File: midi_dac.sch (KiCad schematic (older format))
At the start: 1 part

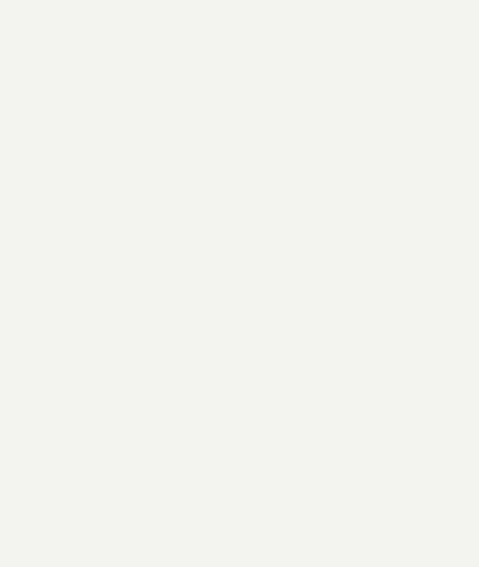
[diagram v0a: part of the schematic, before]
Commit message: Work on user io subsystem schematic
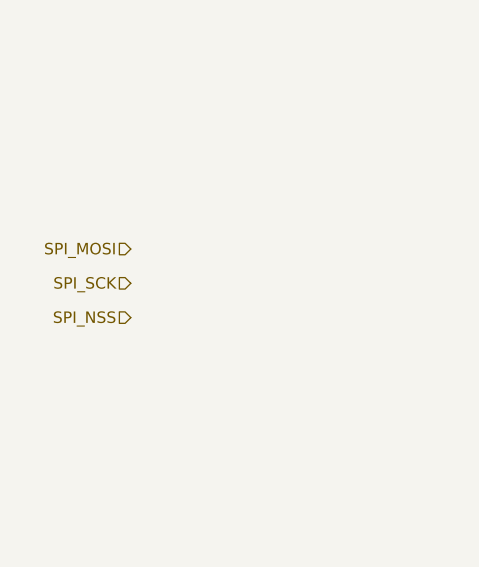
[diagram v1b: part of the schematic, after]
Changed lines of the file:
@@
 	1    0    0    -1
 $EndComp
+Text HLabel 950  2750 0    50   Input ~ 0
+SPI_MOSI
+Text HLabel 950  2900 0    50   Input ~ 0
+SPI_SCK
+Text HLabel 950  3050 0    50   Input ~ 0
+SPI_NSS
 $EndSCHEMATC

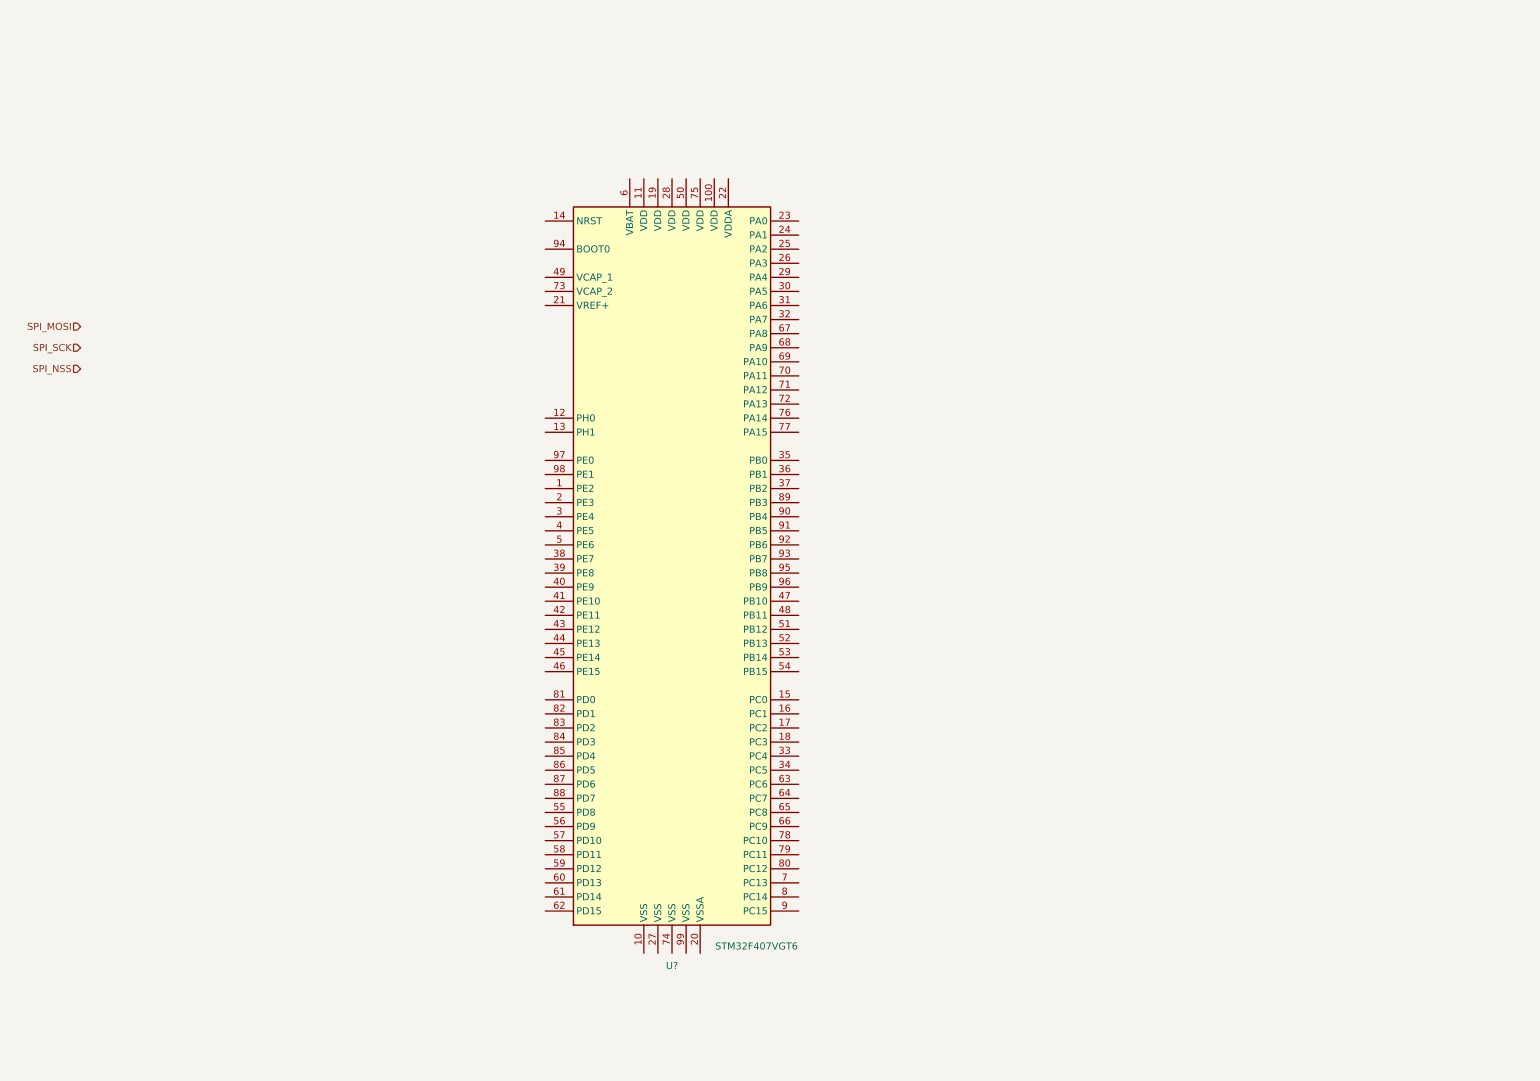
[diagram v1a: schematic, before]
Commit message: Add f4 decoupling capacitors, add dac, add power converter circuit
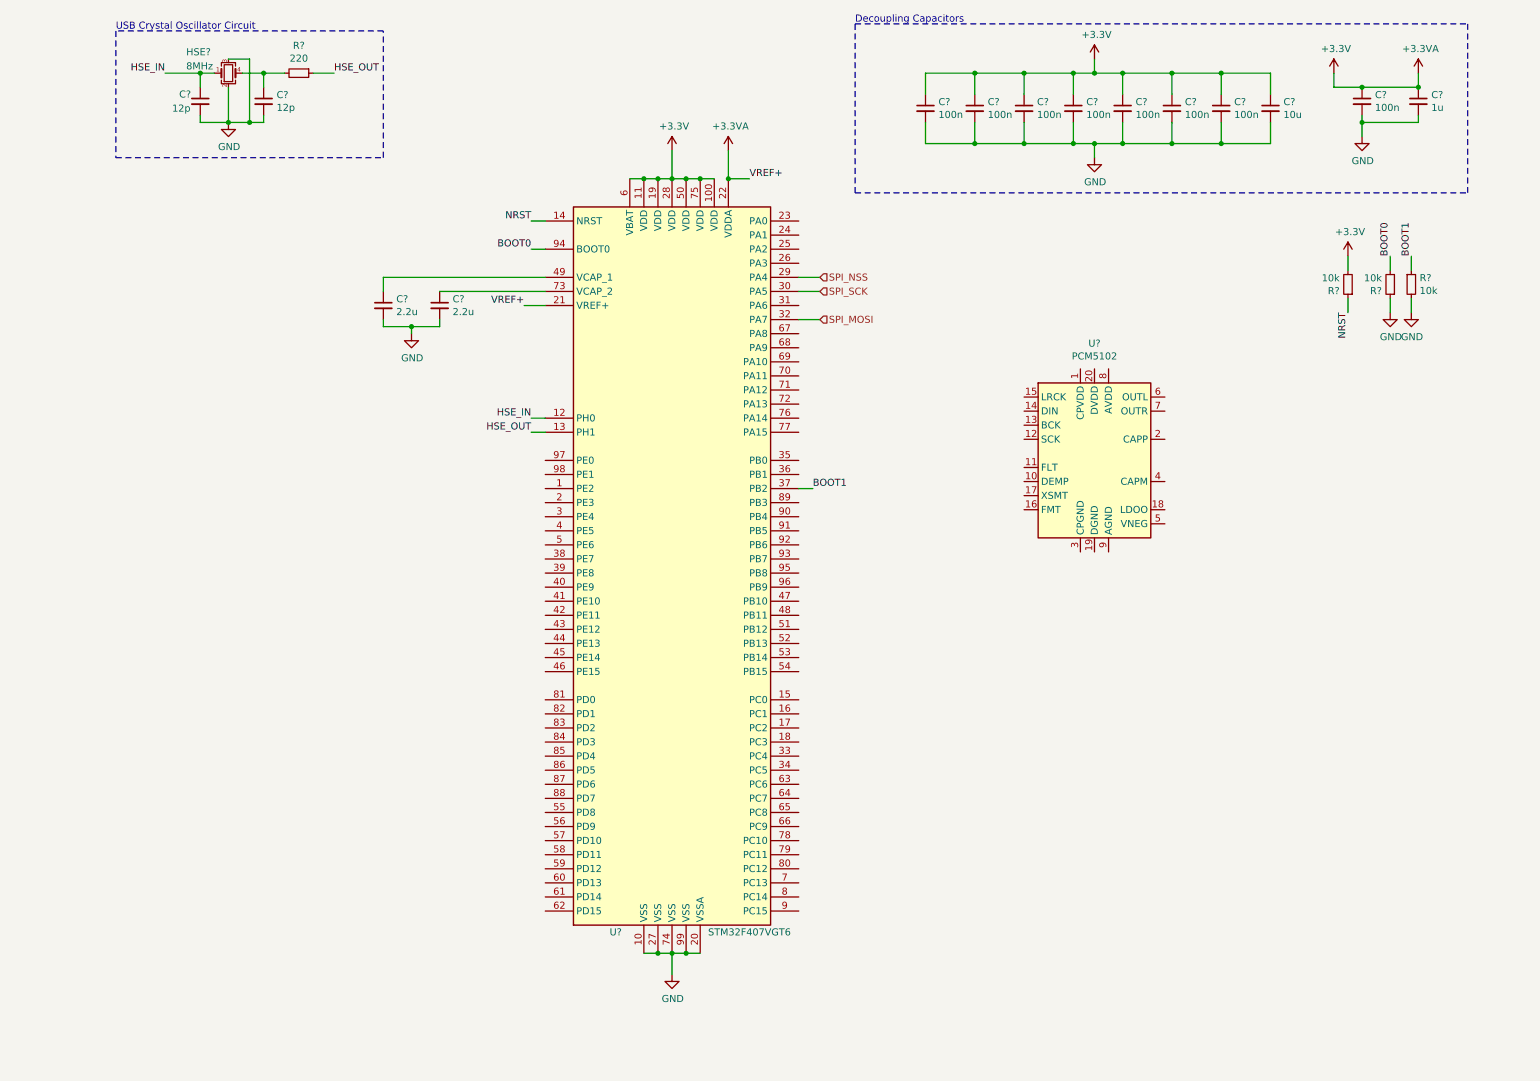
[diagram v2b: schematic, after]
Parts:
- added C? (x8): 100n, symbol Device:C_Small
- added C?: 10u, symbol Device:C_Small
- added C?: 1u, symbol Device:C_Small
- added C? (x2): 2.2u, symbol Device:C_Small
- added C? (x2): 12p, symbol Device:C_Small
- added HSE?: 8MHz, symbol Device:Crystal_GND23_Small
- added R? (x3): 10k, symbol Device:R_Small
- added R?: 220, symbol Device:R_Small
- added U?: PCM5102, Package_SO:TSSOP-20_4.4x6.5mm_P0.65mm, symbol Audio:PCM5102
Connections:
- net SPI_MOSI: now also U?.32 (PA7)
- net SPI_NSS: now also U?.29 (PA4)
- net SPI_SCK: now also U?.30 (PA5)
- net GND: now reaches U?.10 (VSS)
- net GND: now also U?.20 (VSSA), U?.27 (VSS), U?.74 (VSS), U?.99 (VSS), C?.2, C?.2, C?.2, C?.2, C?.2, C?.2, C?.2, C?.2, C?.2, C?.2, C?.2, C?.2, C?.2, C?.2, HSE?.2, HSE?.3, R?.1, R?.2
- net +3.3VA: now reaches U?.100 (VDD)
- net +3.3VA: now also U?.11 (VDD), U?.19 (VDD), U?.21 (VREF+), U?.22 (VDDA), U?.28 (VDD), U?.50 (VDD), U?.6 (VBAT), U?.75 (VDD), C?.1, C?.1, C?.1, C?.1, C?.1, C?.1, C?.1, C?.1, C?.1, C?.1, R?.2
- net HSE_IN: now reaches U?.12 (PH0)
- net HSE_IN: now also C?.1, HSE?.1
- net HSE_OUT: now reaches U?.13 (PH1)
- net HSE_OUT: now also R?.1
- net NRST: now reaches U?.14 (NRST)
- net NRST: now also R?.1
- net BOOT1: now reaches U?.37 (PB2)
- net BOOT1: now also R?.1
- net at U?.49 (VCAP_1): now also C?.1
- net at U?.73 (VCAP_2): now also C?.1
- net BOOT0: now reaches U?.94 (BOOT0)
- net BOOT0: now also R?.2
- new net: C?.1, HSE?.4, R?.2
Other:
- note added: "Decoupling Capacitors"
- note added: "USB Crystal Oscillator Circuit"

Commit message: Finish prototype of DAC/USB/Power system
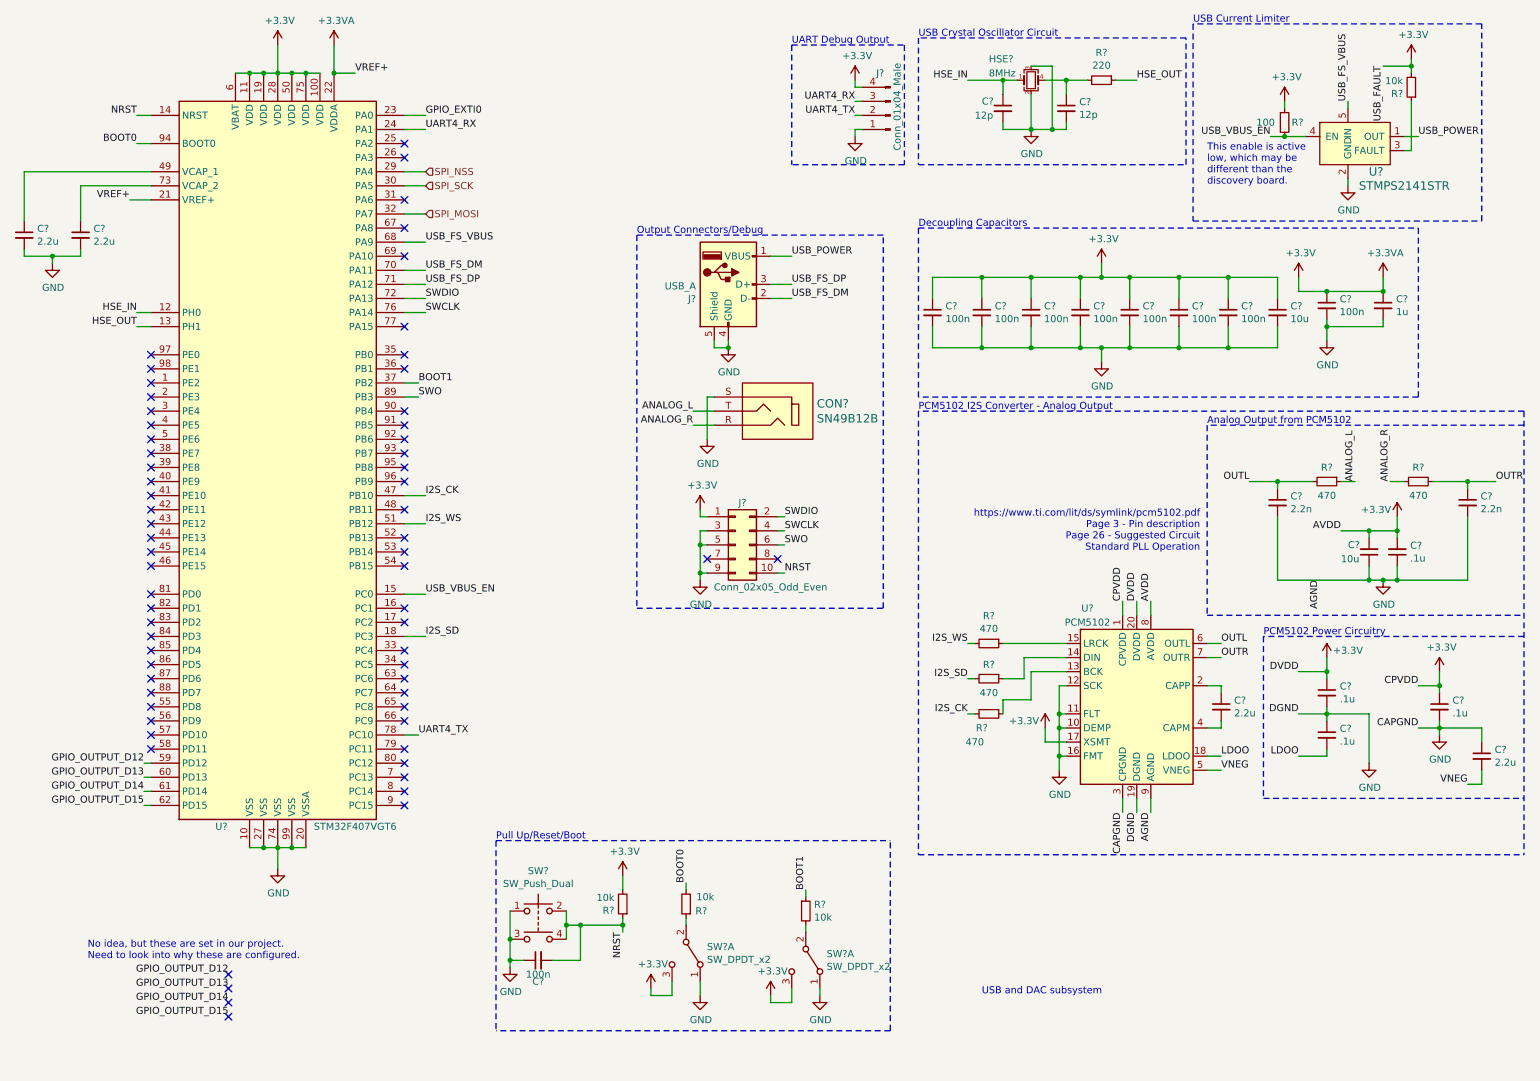
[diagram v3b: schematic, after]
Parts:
- added C? (x4): .1u, symbol Device:C_Small
- added C? (x2): 2.2u, symbol Device:C_Small
- added C? (x2): 2.2n, symbol Device:C_Small
- added C?: 10u, symbol Device:C_Small
- added C?: 100n, symbol Device:C_Small
- added CON?: SN49B12B, digikey-footprints:Headphone_Jack_6.35mm_SN49B12B, symbol DIGIKEY_AUDIO_JACK:SN49B12B
- added J?: Conn_02x05_Odd_Even, symbol Connector_Generic:Conn_02x05_Odd_Even
- added J?: Conn_01x04_Male, symbol Connector:Conn_01x04_Male
- added J?: USB_A, symbol Connector:USB_A
- added R? (x5): 470, symbol Device:R_Small
- added R?: 100, symbol Device:R_Small
- added R?: 10k, symbol Device:R_Small
- added SW?: SW_Push_Dual, symbol Switch:SW_Push_Dual
- added SW? (x2): SW_DPDT_x2, symbol Switch:SW_DPDT_x2
- added U?: STMPS2141STR, digikey-footprints:SOT-753, symbol DIGIKEY_POWER_SWITCH:STMPS2141STR
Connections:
- net +3.3VA: now also U?.1 (CPVDD), U?.17 (XSMT), U?.20 (DVDD), U?.8 (AVDD), C?.1, C?.1, C?.2, C?.2, J?.1 (Pin_1), J?.4 (Pin_4), R?.1, R?.2, SW?.3 (C), SW?.3 (C)
- net GND: now also U?.10 (DEMP), U?.11 (FLT), U?.12 (SCK), U?.16 (FMT), U?.19 (DGND), U?.3 (CPGND), U?.9 (AGND), C?.1, C?.1, C?.1, C?.1, C?.1, C?.2, C?.2, C?.2, C?.2, CON?.S, J?.1 (Pin_1), J?.3 (Pin_3), J?.4 (GND), J?.5 (Pin_5), J?.5 (Shield), J?.9 (Pin_9), SW?.1, SW?.1 (A), SW?.1 (A), SW?.3, U?.2 (GND); no longer R?.1, R?.2
- net NRST: now also C?.2, J?.10 (Pin_10), SW?.2, SW?.4
- net USB_VBUS_EN: now reaches U?.15 (PC0)
- net USB_VBUS_EN: now also R?.2, U?.4 (EN)
- net I2S_SD: now reaches U?.18 (PC3)
- net I2S_SD: now also R?.2
- net GPIO_EXTI0: now reaches U?.23 (PA0)
- net UART4_RX: now reaches U?.24 (PA1)
- net UART4_RX: now also J?.3 (Pin_3)
- net I2S_CK: now reaches U?.47 (PB10)
- net I2S_CK: now also R?.2
- net I2S_WS: now reaches U?.51 (PB12)
- net I2S_WS: now also R?.2
- net GPIO_OUTPUT_D12: now reaches U?.59 (PD12)
- net GPIO_OUTPUT_D13: now reaches U?.60 (PD13)
- net GPIO_OUTPUT_D14: now reaches U?.61 (PD14)
- net GPIO_OUTPUT_D15: now reaches U?.62 (PD15)
- net USB_FS_VBUS: now reaches U?.68 (PA9)
- net USB_FS_VBUS: now also U?.5 (IN)
- net USB_FS_DM: now reaches U?.70 (PA11)
- net USB_FS_DM: now also J?.2 (D-)
- net USB_FS_DP: now reaches U?.71 (PA12)
- net USB_FS_DP: now also J?.3 (D+)
- net SWDIO: now reaches U?.72 (PA13)
- net SWDIO: now also J?.2 (Pin_2)
- net SWCLK: now reaches U?.76 (PA14)
- net SWCLK: now also J?.4 (Pin_4)
- net UART4_TX: now reaches U?.78 (PC10)
- net UART4_TX: now also J?.2 (Pin_2)
- net SWO: now reaches U?.89 (PB3)
- net SWO: now also J?.6 (Pin_6)
- net at U?.13 (BCK): now also R?.1
- net at U?.14 (DIN): now also R?.1
- net at U?.15 (LRCK): now also R?.1
- net LDOO: now reaches U?.18 (LDOO)
- net LDOO: now also C?.2
- net at U?.2 (CAPP): now also C?.1
- net at U?.4 (CAPM): now also C?.2
- net VNEG: now reaches U?.5 (VNEG)
- net VNEG: now also C?.2
- net OUTL: now reaches U?.6 (OUTL)
- net OUTL: now also C?.1, R?.2
- net OUTR: now reaches U?.7 (OUTR)
- net OUTR: now also C?.1, R?.2
- new net: R?.2, SW?.2 (B)
- new net: R?.1, SW?.2 (B)
- new net: R?.1, U?.3 (FAULT)
- new net ANALOG_L: CON?.T, R?.1
- new net ANALOG_R: CON?.R, R?.1
- new net USB_POWER: J?.1 (VBUS), U?.1 (OUT)
- no-connect marks 0 -> 65
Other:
- note added: "Analog Output from PCM5102\n"
- note added: "No idea, but these are set in our project.\nNeed to look into why these are configured.\n"
- note added: "Output Connectors/Debug\n"
- note added: "PCM5102 I2S Converter - Analog Output"
- note added: "PCM5102 Power Circuitry\n"
- note added: "Pull Up/Reset/Boot"
- note added: "This enable is active\nlow, which may be\ndifferent than the\ndiscovery board."
- note added: "UART Debug Output\n"
- note added: "USB Current Limiter"
- note added: "USB and DAC subsystem\n"
- note added: "https://www.ti.com/lit/ds/symlink/pcm5102.pdf\nPage 3 - Pin description\nPage 26 - Suggested Circuit\nStandard PLL Operation"
- moved on the sheet: C?, HSE?, R?, U?

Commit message: Finish screen subsystem
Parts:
- C? (x2): value 12p -> 20p
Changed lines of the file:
@@
 P 7950 1200
 F 0 "C?" H 8042 1246 50  0000 L CNN
-F 1 "12p" H 8042 1155 50  0000 L CNN
+F 1 "20p" H 8042 1155 50  0000 L CNN
 F 2 "" H 7950 1200 50  0001 C CNN
 F 3 "~" H 7950 1200 50  0001 C CNN
@@
 P 7500 1200
 F 0 "C?" H 7350 1250 50  0000 L CNN
-F 1 "12p" H 7300 1150 50  0000 L CNN
+F 1 "20p" H 7300 1150 50  0000 L CNN
 F 2 "" H 7500 1200 50  0001 C CNN
 F 3 "~" H 7500 1200 50  0001 C CNN

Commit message: Add one more debug connector
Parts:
- added J?: Conn_01x03_Male, symbol Connector:Conn_01x03_Male
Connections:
- net ANALOG_L: now also J?.3 (Pin_3)
- net ANALOG_R: now also J?.2 (Pin_2)
- net GND: now also J?.1 (Pin_1)
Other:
- note added: "Debug Connections"
- note added: "Output Connectors\n"
- note removed: "Output Connectors/Debug\n"
- note removed: "UART Debug Output\n"
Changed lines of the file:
@@
 	6450 1150 6500 1150
 Wire Notes Line
-	6000 750  6800 750
-Wire Notes Line
 	6800 750  6800 1600
-Wire Notes Line
-	6800 1600 6000 1600
-Wire Notes Line
-	6000 750  6000 1600
-Text Notes 6000 750  0    50   ~ 0
-UART Debug Output\n
 Text Label 3400 2450 0    50   ~ 0
 USB_FS_DP
@@
 	4900 2100 4900 4750
 Text Notes 4900 2100 0    50   ~ 0
-Output Connectors/Debug\n
+Output Connectors\n
 NoConn ~ 3250 1450
 NoConn ~ 3250 1550
@@
 NoConn ~ 1450 3050
 NoConn ~ 1450 2950
-Text Label 2000 7650 2    50   ~ 0
+Text Label 2100 7550 2    50   ~ 0
 GPIO_OUTPUT_D15
-Text Label 2000 7550 2    50   ~ 0
+Text Label 2100 7450 2    50   ~ 0
 GPIO_OUTPUT_D14
-Text Label 2000 7450 2    50   ~ 0
+Text Label 2100 7350 2    50   ~ 0
 GPIO_OUTPUT_D13
-Text Label 2000 7350 2    50   ~ 0
+Text Label 2100 7250 2    50   ~ 0
 GPIO_OUTPUT_D12
-NoConn ~ 2000 7350
-NoConn ~ 2000 7450
-NoConn ~ 2000 7550
-NoConn ~ 2000 7650
-Text Notes 1000 7250 0    50   ~ 0
+NoConn ~ 2100 7250
+NoConn ~ 2100 7350
+NoConn ~ 2100 7450
+NoConn ~ 2100 7550
+Text Notes 1100 7150 0    50   ~ 0
 No idea, but these are set in our project.\nNeed to look into why these are configured.\n
 $Comp
@@
 Text Notes 7350 7500 0    50   ~ 0
 USB and DAC subsystem\n
+$Comp
+L Connector:Conn_01x03_Male J?
+U 1 1 604E0612
+P 5850 1150
+F 0 "J?" H 6100 950 50  0000 R CNN
+F 1 "Conn_01x03_Male" H 6200 1450 50  0000 R CNN
+F 2 "" H 5850 1150 50  0001 C CNN
+F 3 "~" H 5850 1150 50  0001 C CNN
+	1    5850 1150
+	-1   0    0    1
+$EndComp
+$Comp
+L power:GND #PWR?
+U 1 1 604E24D2
+P 5500 1300
+F 0 "#PWR?" H 5500 1050 50  0001 C CNN
+F 1 "GND" H 5400 1200 50  0000 C CNN
+F 2 "" H 5500 1300 50  0001 C CNN
+F 3 "" H 5500 1300 50  0001 C CNN
+	1    5500 1300
+	1    0    0    -1
+$EndComp
+Wire Wire Line
+	5500 1300 5500 1250
+Wire Wire Line
+	5500 1250 5650 1250
+Text Label 5500 1050 2    50   ~ 0
+ANALOG_L
+Text Label 5500 1150 2    50   ~ 0
+ANALOG_R
+Wire Wire Line
+	5500 1050 5650 1050
+Wire Wire Line
+	5500 1150 5650 1150
+Wire Notes Line
+	5100 1600 5100 750
+Wire Notes Line
+	5100 750  6800 750
+Wire Notes Line
+	5100 1600 6800 1600
+Text Notes 5100 750  0    50   ~ 0
+Debug Connections
 $EndSCHEMATC

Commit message: Make updates per suggestions
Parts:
- removed R?: 10k, symbol Device:R_Small
- removed R? (x3): 470, symbol Device:R_Small
- removed SW? (x2): SW_DPDT_x2, symbol Switch:SW_DPDT_x2
- added C23, C24, C47: 100n, symbol Device:C_Small
- added C44: 4.7u, symbol Device:C_Small
- added D2: BLUE_LED, symbol Device:LED
- added D3: GREEN_LED, symbol Device:LED
- added D4, D5: LED, symbol Device:LED
- added J9: Conn_01x05_Male, symbol Connector:Conn_01x05_Male
- added R25: 50, symbol Device:R_Small
- added R26: 60, symbol Device:R_Small
- added R27: 65, symbol Device:R_Small
- added R28: 67.5, symbol Device:R_Small
- added R29, R30, R31: 470, symbol Device:R_Small
- added R34, R35: 22, symbol Device:R_Small
- added R36, R37, R38, R39, R40, R41: 10k, symbol Device:R_Small
- added SW5, SW6: SW_Push_Dual, symbol Switch:SW_Push_Dual
- R43: renamed from R?; value 100 -> 10k
- gave numbers to parts that had none: 40
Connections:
- net +3.3VA: now also C23.1, C24.1, C47.1, J9.5 (Pin_5), R37.1, SW5.1, SW5.3, SW6.1, SW6.3; no longer C40.2, C42.2, U6.17 (XSMT), U6.8 (AVDD)
- net BOOT0: now also R33.1, C23.2, SW5.2, SW5.4; no longer R33.2
- net BOOT1: now also C24.2, R36.1, SW6.2, SW6.4
- net GND: now also R33.2, C44.2, C47.2, J9.1 (Pin_1), R25.1, R26.1, R27.1, R28.1, R36.2, R38.2, R39.2, R40.2, R41.2; no longer U6.10 (DEMP), U6.11 (FLT), U6.12 (SCK), U6.16 (FMT)
- net GPIO_OUTPUT_D12: now also D2.2 (A)
- net GPIO_OUTPUT_D13: now also D3.2 (A)
- net GPIO_OUTPUT_D14: now also D4.2 (A)
- net GPIO_OUTPUT_D15: now also D5.2 (A)
- net I2S_CK: now also U6.13 (BCK), J9.3 (Pin_3), R29.1; no longer U5.47 (PB10)
- net I2S_SD: now also U6.14 (DIN), J9.2 (Pin_2), R31.1; no longer U5.18 (PC3)
- net I2S_WS: now also U6.15 (LRCK), J9.4 (Pin_4), R30.1; no longer U5.51 (PB12)
- net USB_FS_DM: now also R35.1; no longer J10.2 (D-)
- net USB_FS_DP: now also R34.1; no longer J10.3 (D+)
- net USB_POWER: now also C44.1
- net SOFT_MUTE: now reaches U5.34 (PC5)
- net SOFT_MUTE: now also U6.17 (XSMT), R37.2
- net SPI_INT: now reaches U5.90 (PB4)
- net USB_FAULT: now reaches R46.1, U7.3 (FAULT)
- new net: R31.2, U5.18 (PC3)
- new net: R29.2, U5.47 (PB10)
- new net: R30.2, U5.51 (PB12)
- new net: R40.1, U6.10 (DEMP)
- new net: R39.1, U6.11 (FLT)
- new net: R38.1, U6.12 (SCK)
- new net: R41.1, U6.16 (FMT)
- new net: J10.2 (D-), R35.2
- new net: J10.3 (D+), R34.2
- new net: D2.1 (K), R25.2
- new net: D3.1 (K), R26.2
- new net: D4.1 (K), R27.2
- new net: D5.1 (K), R28.2
- new net +3.3VADC: C40.2, C42.2, U6.8 (AVDD)
- no-connect marks 65 -> 59
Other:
- note removed: "No idea, but these are set in our project.\nNeed to look into why these are configured.\n"
- moved on the sheet: C22, C25, C26, C27, C28, C29, C30, C31, C32, C33, C34, C35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
